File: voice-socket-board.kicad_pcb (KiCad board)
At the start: 2 copper layers, 150 x 100 mm, 275 parts, among them J1 JACK_MONO_SW, J2 JACK_MONO_SW, J3 JACK_MONO_SW, P1 CONN_01X03, P2 CONN_01X03, P3 CONN_02X05, P4 DDR3-DIMM, Q1 MMBT3904, Q2 DMMT3904W, Q3 2N7002, Q4 2N7002, Q5 MMBT3904, Q6 2N3906, Q7 MMBT3904, Q8 MMBT3904, Q9 MMBT3904, SW1 SPST, SW10 SP3T, SW11 SP3T, SW12 SP3T, SW13 SP3T, SW14 SPST, SW15 TACT_SWITCH, SW2 SPST, SW3 SP3T, SW4 SP3T, SW5 SPST, SW6 SPST, SW7 Switch_SPDT_x2, SW8 2P3T, SW9 SP3T, U1 LM833, U10 TL072-, U11 NE5534, U2 TL072-, U3 TL072-, U4 TL072-, U5 TL072-, U6 TL072-, U7 MAX9945, U8 CD4013, U9 TL072-

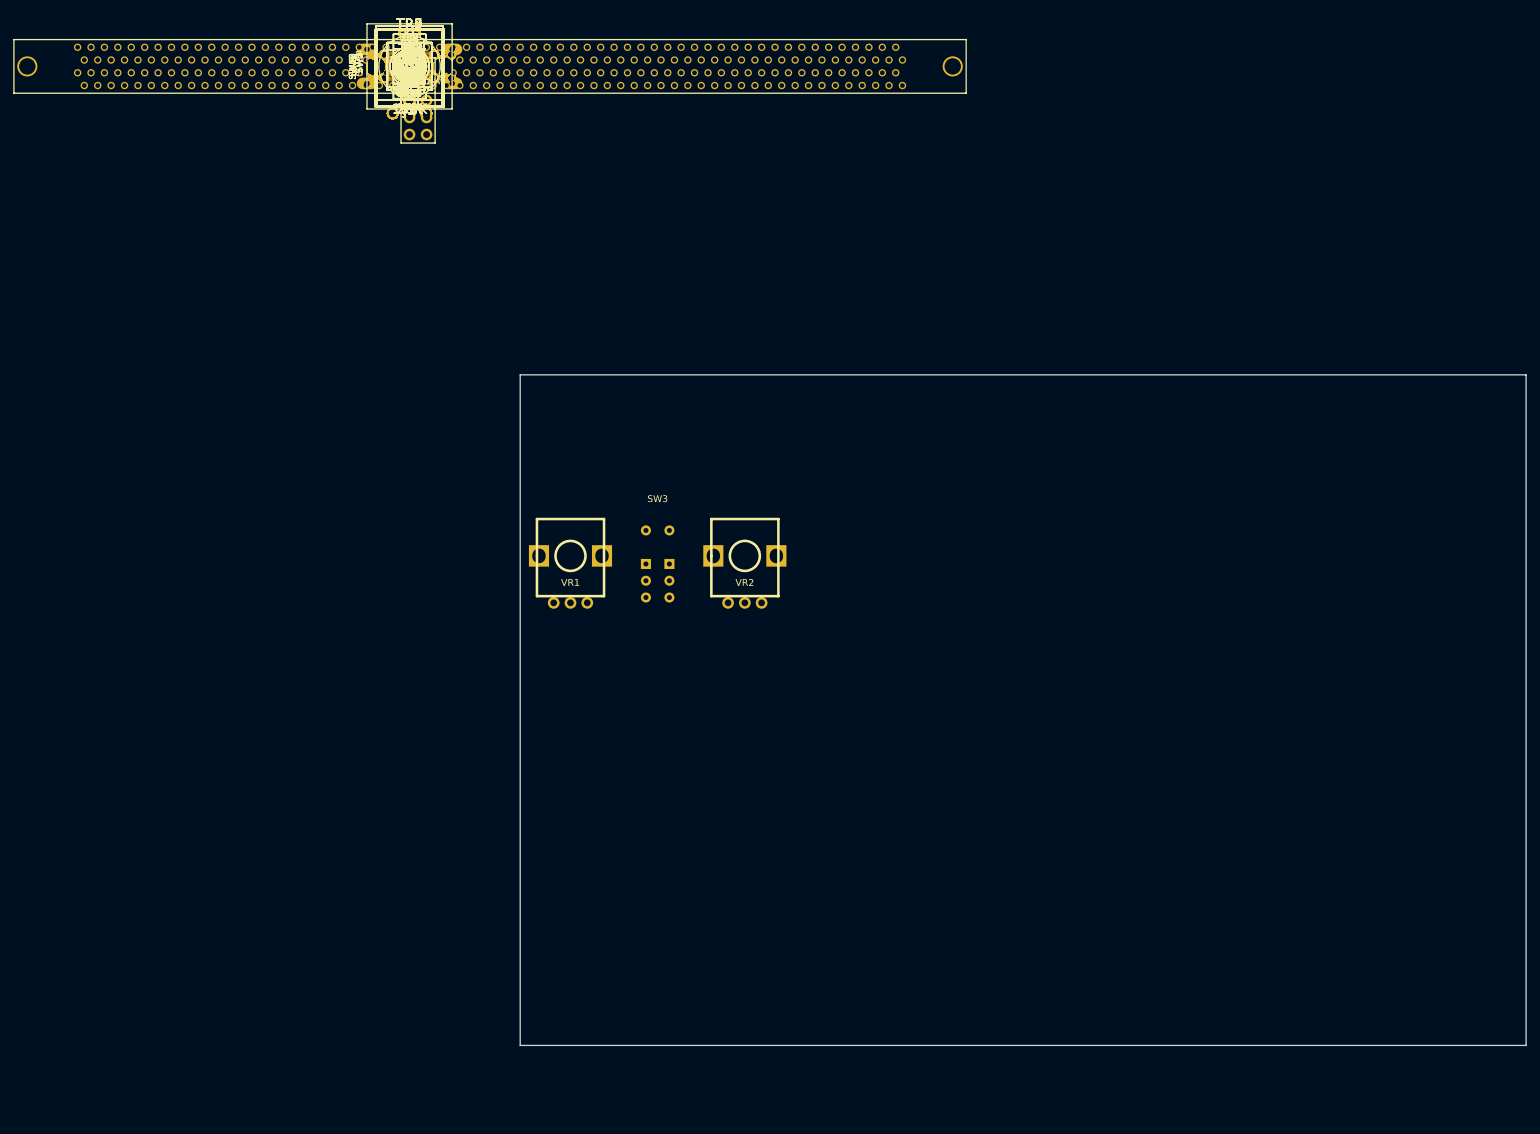
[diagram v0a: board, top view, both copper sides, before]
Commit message: switches, pots and jacks placed. about to move DIMM connector to center of board and see if that works
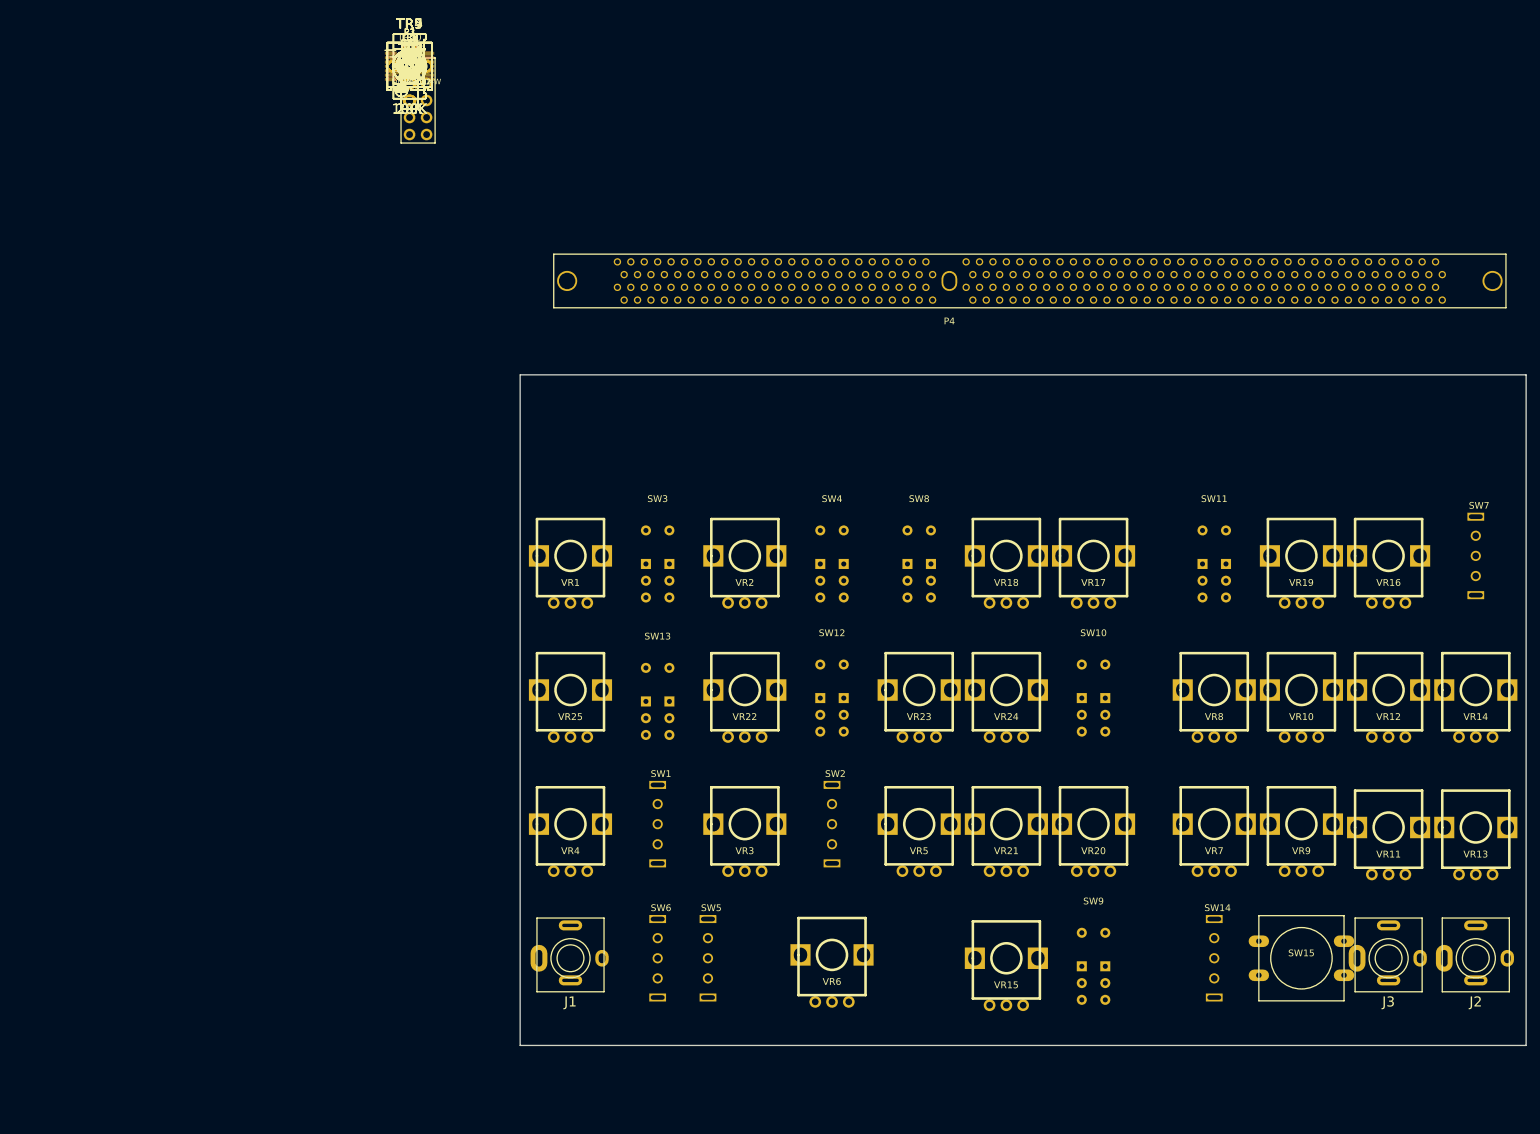
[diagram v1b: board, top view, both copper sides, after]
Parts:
- moved J2 207.3 mm to (187.5, 127.0)
- moved J3 197.5 mm to (174.5, 127.0)
- moved VR13 195.4 mm to (187.5, 107.5)
- moved SW15 188.1 mm to (161.5, 127.0)
- moved VR11 184.9 mm to (174.5, 107.5)
- moved VR14 184.2 mm to (187.5, 87.0)
- moved SW14 179.1 mm to (148.5, 127.0), turned to 270 degrees
- moved SW7 175.0 mm to (187.5, 67.0), turned to 270 degrees
- moved VR9 174.5 mm to (161.5, 107.0)
- moved VR12 173.1 mm to (174.5, 87.0)
- moved SW9 167.6 mm to (130.5, 127.0), turned to 270 degrees
- moved VR7 164.8 mm to (148.5, 107.0)
- moved VR16 163.2 mm to (174.5, 67.0)
- moved VR10 162.3 mm to (161.5, 87.0)
- moved VR15 160.0 mm to (117.5, 127.0)
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
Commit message: placed trimmers
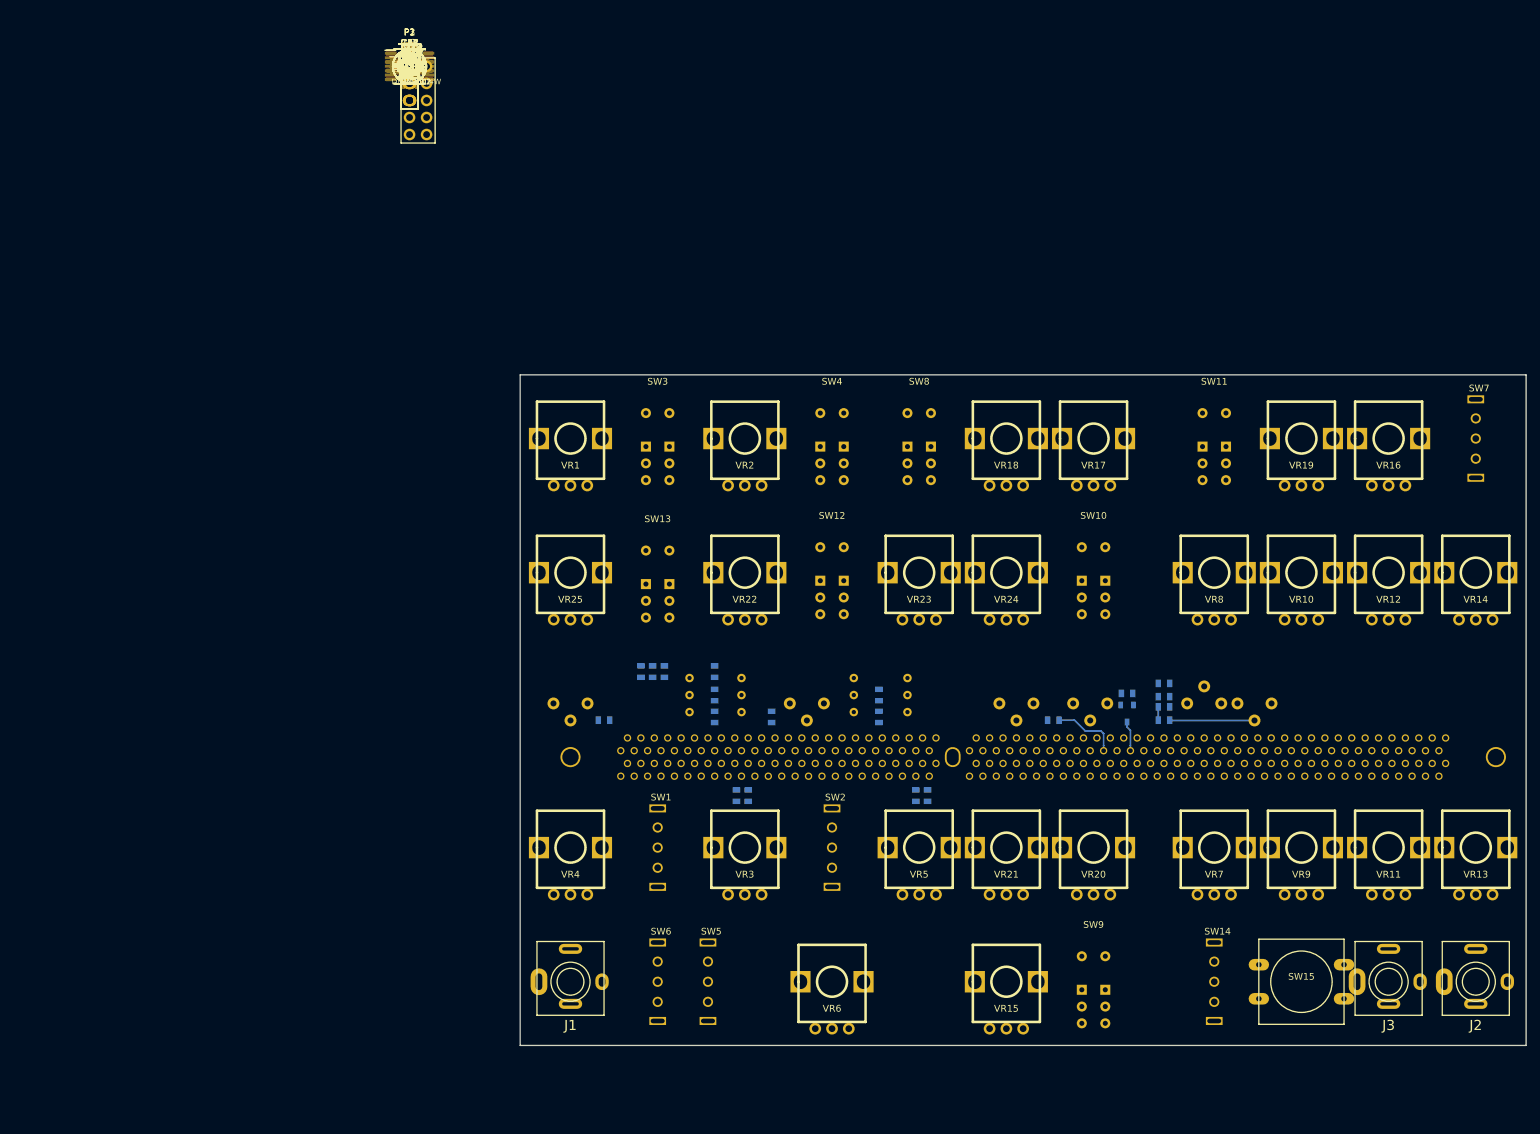
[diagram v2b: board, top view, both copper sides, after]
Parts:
- C58, P4, Q6, R1, R10, R105, R106, R107, R108, R11, R13, R17, R18, R2, R3, R4, R5, R6, R7, R78, R8, R9, TR1, TR10, TR2, TR3, TR4, TR5, TR6, TR7, TR8, TR9: moved to B.Cu
- moved TR3 157.8 mm to (154.5, 89.0)
- moved TR2 151.9 mm to (147.0, 89.0), turned to 180 degrees
- moved R107 148.9 mm to (141.0, 91.5)
- moved R108 147.6 mm to (141.0, 89.5)
- moved C58 146.6 mm to (141.0, 88.0), turned to 180 degrees
- moved R106 145.3 mm to (141.0, 86.0), turned to 180 degrees
- moved Q6 144.1 mm to (135.5, 90.5)
- moved R105 142.1 mm to (135.5, 87.5), turned to 180 degrees
- moved TR1 139.0 mm to (130.0, 89.0)
- moved R78 136.8 mm to (124.5, 91.5)
- moved R11 133.4 mm to (105.8, 102.8), turned to 270 degrees
- moved R10 132.4 mm to (104.0, 102.8), turned to 270 degrees
- moved TR10 131.2 mm to (119.0, 89.0)
- moved R1 119.9 mm to (79.0, 102.8), turned to 270 degrees
- moved R17 119.6 mm to (98.5, 91.0), turned to 90 degrees
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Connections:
- C2 pad 1: VCO1_SCALE -> VCO2_SCALE
- C2 pad 2: VCO1_PITCH_CV -> VCO2_PITCH_CV
- R10 pad 1: VCO1_PITCH_CV -> VCO2_PITCH_CV
- R11 pad 1: VCO1_PITCH_CV -> VCO2_PITCH_CV
- R12 pad 1: VCO1_PITCH_CV -> VCO2_PITCH_CV
- R13 pad 1: VCO1_PITCH_CV -> VCO2_PITCH_CV
- R14 pad 1: VCO1_PITCH_CV -> VCO2_PITCH_CV
- R15 pad 1: VCO1_PITCH_CV -> VCO2_PITCH_CV
- R16 pad 1: VCO1_PITCH_CV -> VCO2_PITCH_CV
- R17 pad 1: VCO1_SCALE -> VCO2_SCALE
- R18 pad 1: VCO1_TRI_SHAPE -> VCO2_TRI_SHAPE
- TR9 pad 1: VCO1_PITCH_CV -> VCO2_PITCH_CV
- TR9 pad 2: VCO1_PITCH_CV -> VCO2_PITCH_CV
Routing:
- net Net-(R107-Pad2): track 0.00 -> 12.7 mm
- net VCA_IN: track 0.00 -> 10.0 mm
- net RES_CTRL: track 0.00 -> 4.49 mm
- net VCF_CTRL: track 0.00 -> 2.00 mm
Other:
- net class Default: clearance 0.2 -> 0.2032; trace_width 0.25 -> 0.254; via_dia 0.6 -> 1.016; via_drill 0.4 -> 0.508
- net class POWER added: clearance 0.2032, trace_width 0.3048, via_dia 1.016, via_drill 0.508
- rule trace_clearance: 0.2 -> 0.2032

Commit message: placing components
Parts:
- C1, C2, C57, C59, R100, R101, R102, R109, R110, R111, R113, R14, R15, R16, R97, R98, R99, TP5, U10: moved to B.Cu
- C60: footprint MyModules:SM0603-C-JRL -> MyModules:2MM-POL-CAP; moved to B.Cu
- moved R101 132.7 mm to (126.5, 83.5), turned to 90 degrees
- moved R97 131.4 mm to (124.8, 83.5), turned to 90 degrees
- moved R14 131.4 mm to (102.2, 102.8), turned to 270 degrees
- moved C57 130.5 mm to (117.5, 89.5), turned to 90 degrees
- moved R98 130.2 mm to (123.0, 83.5), turned to 90 degrees
- moved R102 129.4 mm to (115.8, 89.5), turned to 270 degrees
- moved TP5 129.0 mm to (112.8, 91.8)
- moved R100 128.9 mm to (121.2, 83.5), turned to 90 degrees
- moved C59 127.8 mm to (113.5, 89.5), turned to 90 degrees
- moved R99 127.6 mm to (119.5, 83.5), turned to 90 degrees
- moved R113 126.7 mm to (111.8, 89.5), turned to 270 degrees
- moved U10 125.4 mm to (114.5, 85.2), turned to 90 degrees
- moved C60 124.6 mm to (108.0, 90.0), turned to 180 degrees
- moved R110 120.5 mm to (108.0, 84.5), turned to 270 degrees
- moved R109 119.3 mm to (106.2, 84.5), turned to 270 degrees
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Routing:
- net VCA_IN: track 10.0 -> 0.00 mm
- net RES_CTRL: track 4.49 -> 0.00 mm

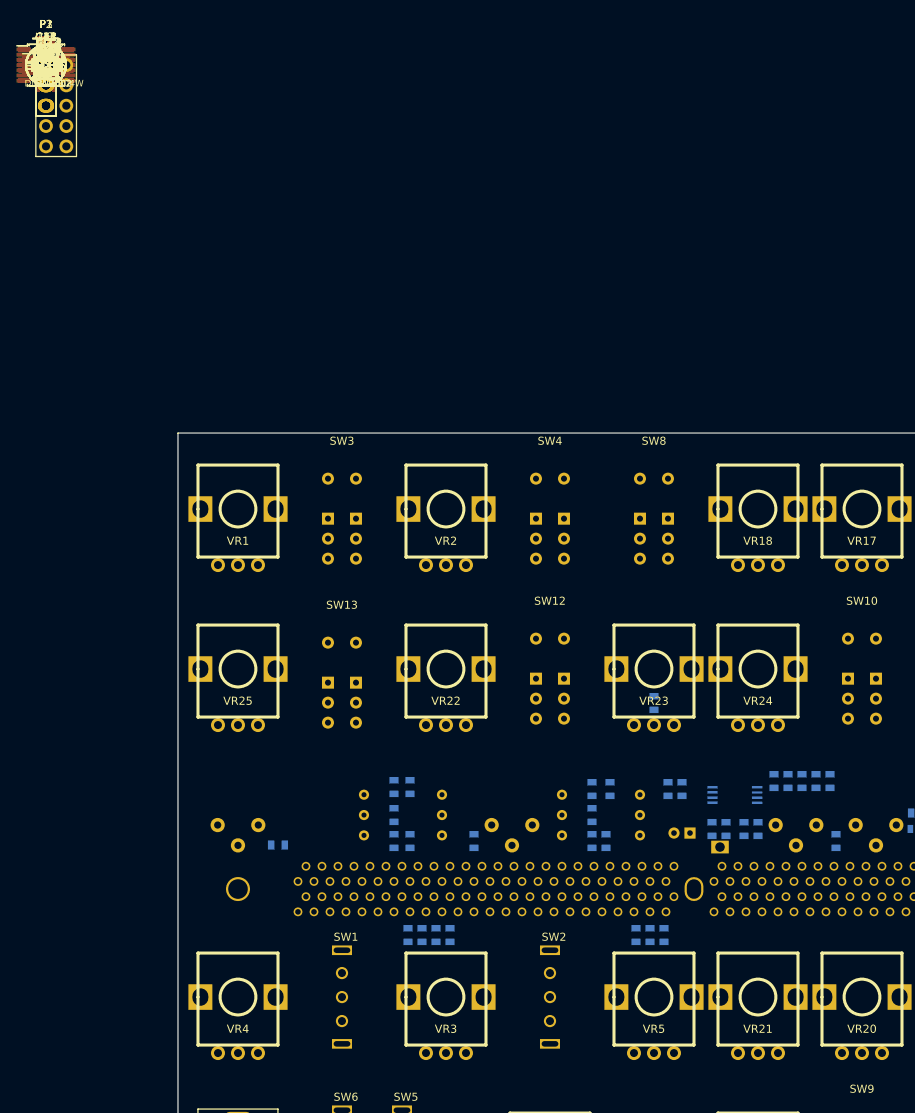
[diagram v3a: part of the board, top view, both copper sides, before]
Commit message: placing components. placed PWM components
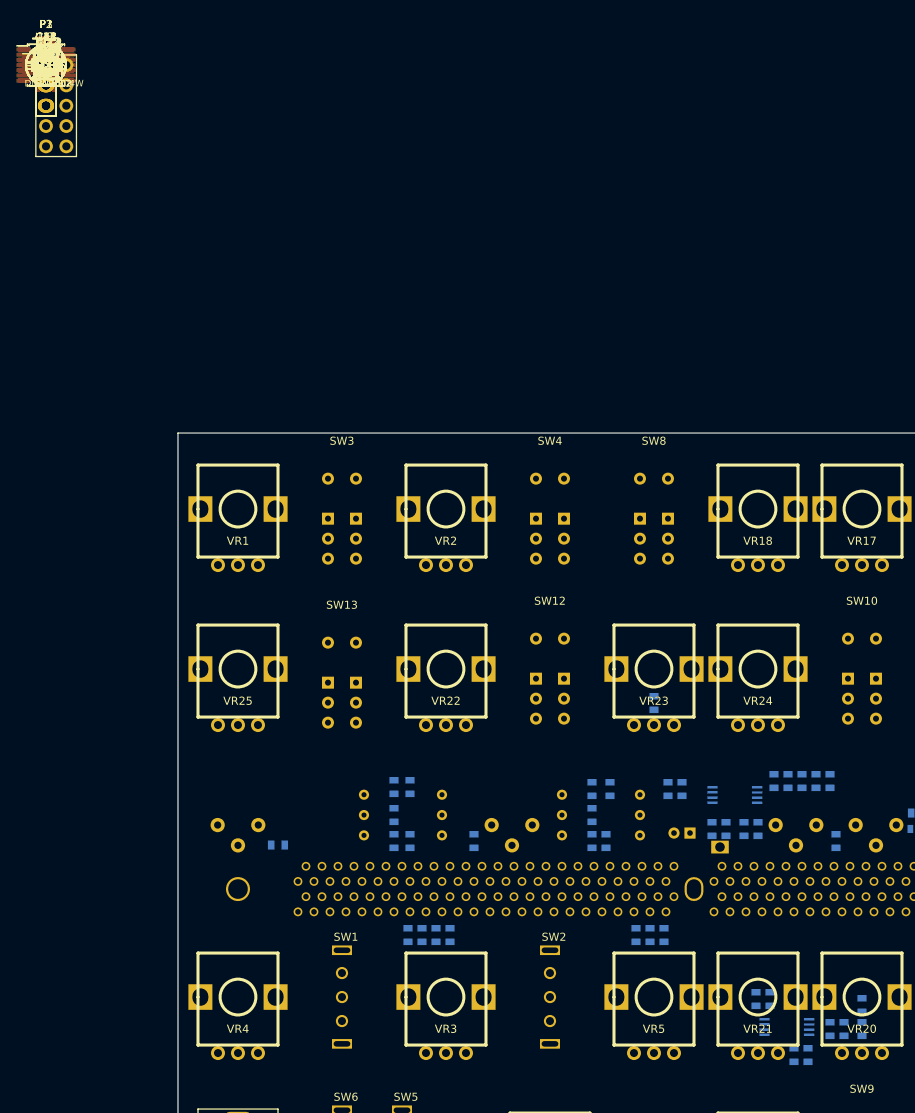
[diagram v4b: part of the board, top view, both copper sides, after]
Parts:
- C54, R84, R85, R86, R89, R90, R91, R92, U9: moved to B.Cu
- moved R91 157.9 mm to (130.5, 114.5), turned to 270 degrees
- moved C54 156.4 mm to (128.2, 114.5), turned to 270 degrees
- moved R85 156.2 mm to (123.8, 117.8), turned to 270 degrees
- moved R90 155.6 mm to (130.5, 111.5), turned to 90 degrees
- moved R92 155.3 mm to (126.5, 114.5), turned to 90 degrees
- moved R89 155.1 mm to (122.0, 117.8), turned to 90 degrees
- moved U9 151.7 mm to (121.0, 114.2), turned to 90 degrees
- moved R86 147.7 mm to (119.0, 110.8), turned to 90 degrees
- moved R84 146.6 mm to (117.2, 110.8), turned to 90 degrees
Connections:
- U9 pad 1: VCO1_PWM_CV -> Net-(R89-Pad1)
- U9 pad 2: Net-(C54-Pad1) -> Net-(R85-Pad1)
- U9 pad 3: GND -> Net-(R84-Pad2)
- U9 pad 5: Net-(R84-Pad2) -> GND
- U9 pad 6: Net-(R85-Pad1) -> Net-(C54-Pad1)
- U9 pad 7: Net-(R89-Pad1) -> VCO1_PWM_CV
